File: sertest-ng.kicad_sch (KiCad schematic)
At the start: 52 parts, among them J101 SWD, J102 USB, SW101 Reset, U101 M24C64-RMN, U102 AMS1117-3.3, U103 STM32G431RBTx, U104 ATECC608B-MAVDA-S, U105 USBLC6-2SC6, Y101 8MHz, Y102 32k

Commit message: Swap USART1 RX/TX
Signed-off-by: Benedikt Spranger <b.spranger@linutronix.de>
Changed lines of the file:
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@@
 	)
 	(label "USART1_TX"
-		(at 226.06 134.62 180)
+		(at 226.06 132.08 180)
 		(effects
 			(font
@@
 	)
 	(label "USART1_RX"
-		(at 226.06 132.08 180)
-		(effects
-			(font
+		(at 226.06 134.62 180)
+		(effects
+			(font

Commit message: Fix USB signal swap
Signed-off-by: Benedikt Spranger <bene@eurovibes.org>
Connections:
- net USB_DM: now also U105.3 (I/O2); no longer U105.1 (I/O1)
- net USB_DP: now also U105.1 (I/O1); no longer U105.3 (I/O2)
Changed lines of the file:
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@@
 	)
 	(label "USB_DM"
-		(at 82.55 149.86 0)
+		(at 82.55 152.4 0)
 		(effects
 			(font
@@
 	)
 	(label "USB_DP"
-		(at 82.55 152.4 0)
+		(at 82.55 149.86 0)
 		(effects
 			(font

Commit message: Add USB termination resistors
Signed-off-by: Benedikt Spranger <b.spranger@linutronix.de>
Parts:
- added R108, R109: 33, Resistor_SMD:R_0402_1005Metric, symbol Device:R
- renumbered C107 to C101, C113 to C102, C114 to C103, C115 to C104, C106 to C105, C105 to C106, C108 to C107, C116 to C108, C101 to C110, C102 to C111, C110 to C112, C103 to C113, C111 to C114, C104 to C115, C112 to C116, D103 to D102, D104 to D103, D105 to D104, D106 to D105, D102 to D106, FB102 to FB101, FB101 to FB102, J102 to J101, J101 to J102, JP102 to JP101, JP101 to JP102, R111 to R102, R112 to R103, R105 to R104, R106 to R105, R104 to R106, R102 to R107, R107 to R110, R108 to R111, R109 to R112, R110 to R113, R103 to R114, U105 to U102, U102 to U105
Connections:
- net USB_DM: now also R109.1; no longer U102.3 (I/O2)
- net USB_DP: now also R108.2; no longer U102.1 (I/O1)
- new net: R108.1, U102.1 (I/O1)
- new net: R109.2, U102.3 (I/O2)

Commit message: Add BOOT0 support
Signed-off-by: Benedikt Spranger <b.spranger@linutronix.de>
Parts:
- added JP103: BOOT0, Jumper:SolderJumper-2_P1.3mm_Open_Pad1.0x1.5mm, symbol Jumper:Jumper_2_Open
- added R115: 10k, Resistor_SMD:R_0402_1005Metric, symbol Device:R
- R108, R109: Long Description (none) -> -55℃~+155℃ 33Ω 50V 62.5mW Thick Film Resistor ±1% ±100ppm/℃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; MF (none) -> UNI-ROYAL(Uniroyal Elec); MP (none) -> 0402WGF330JTCE; SupplLink (none) -> https://jlcpcb.com/partdetail/25848-0402WGF330JTCE/C25105; lcsc# (none) -> C25105
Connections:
- net +3V3: now also JP103.1 (A)
- net FDCAN1_RX: now also JP103.2 (B), R115.1
- net GND: now also R115.2

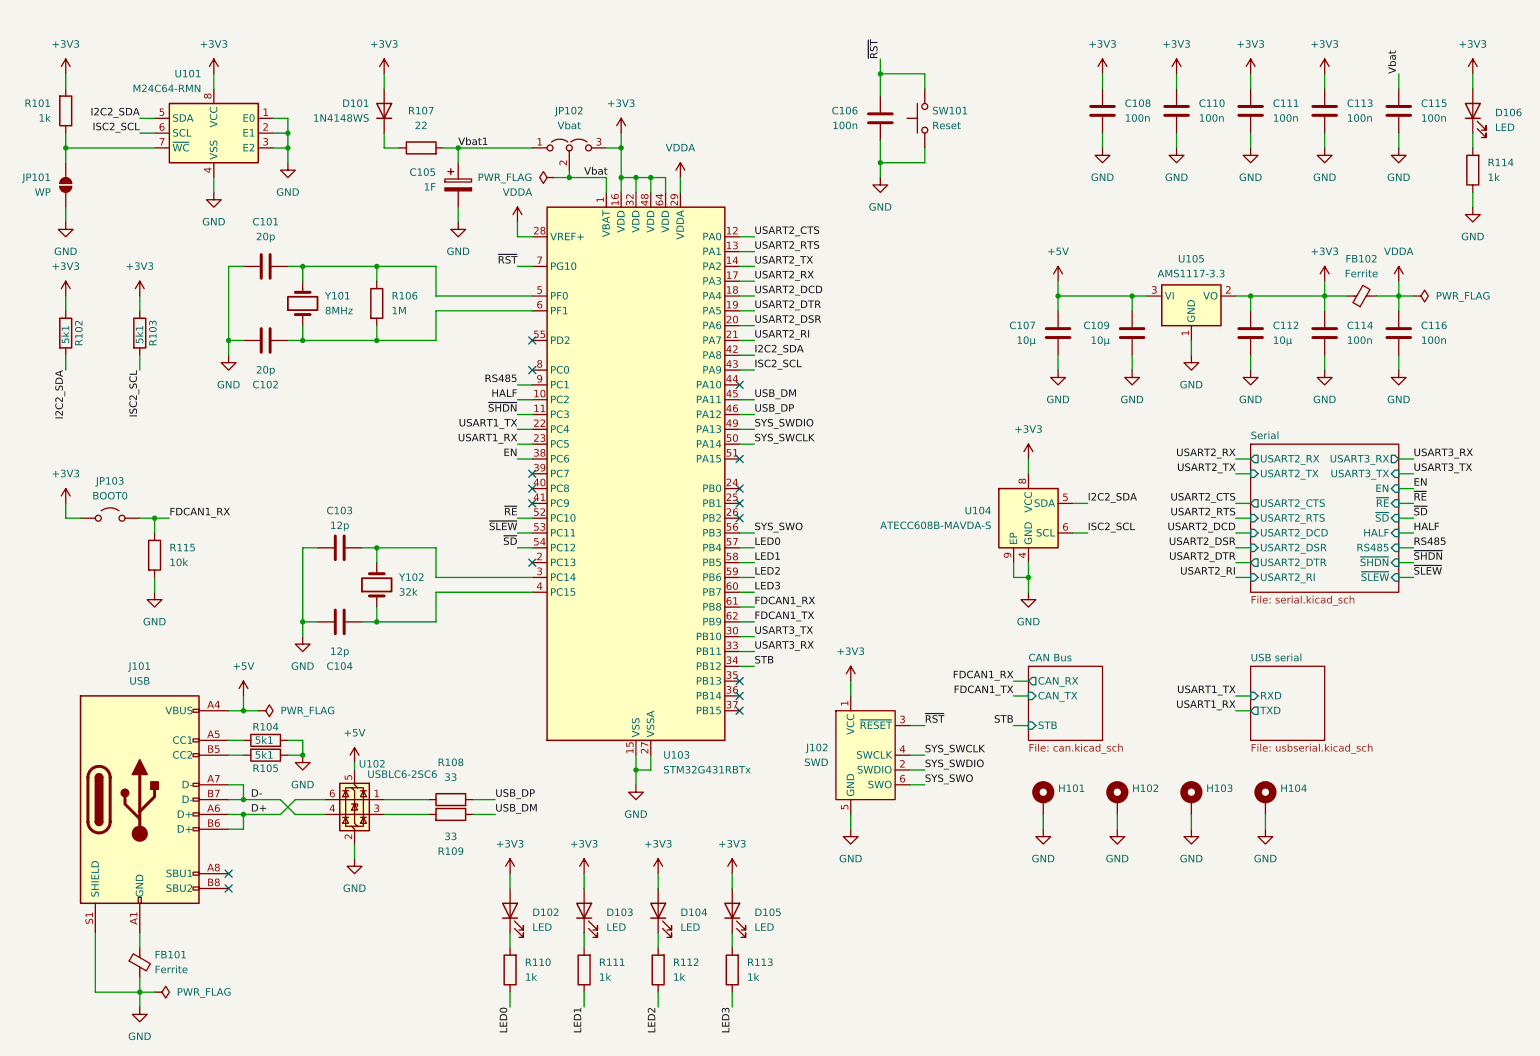
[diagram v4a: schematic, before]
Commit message: Add second EEPROM
Signed-off-by: Benedikt Spranger <b.spranger@linutronix.de>
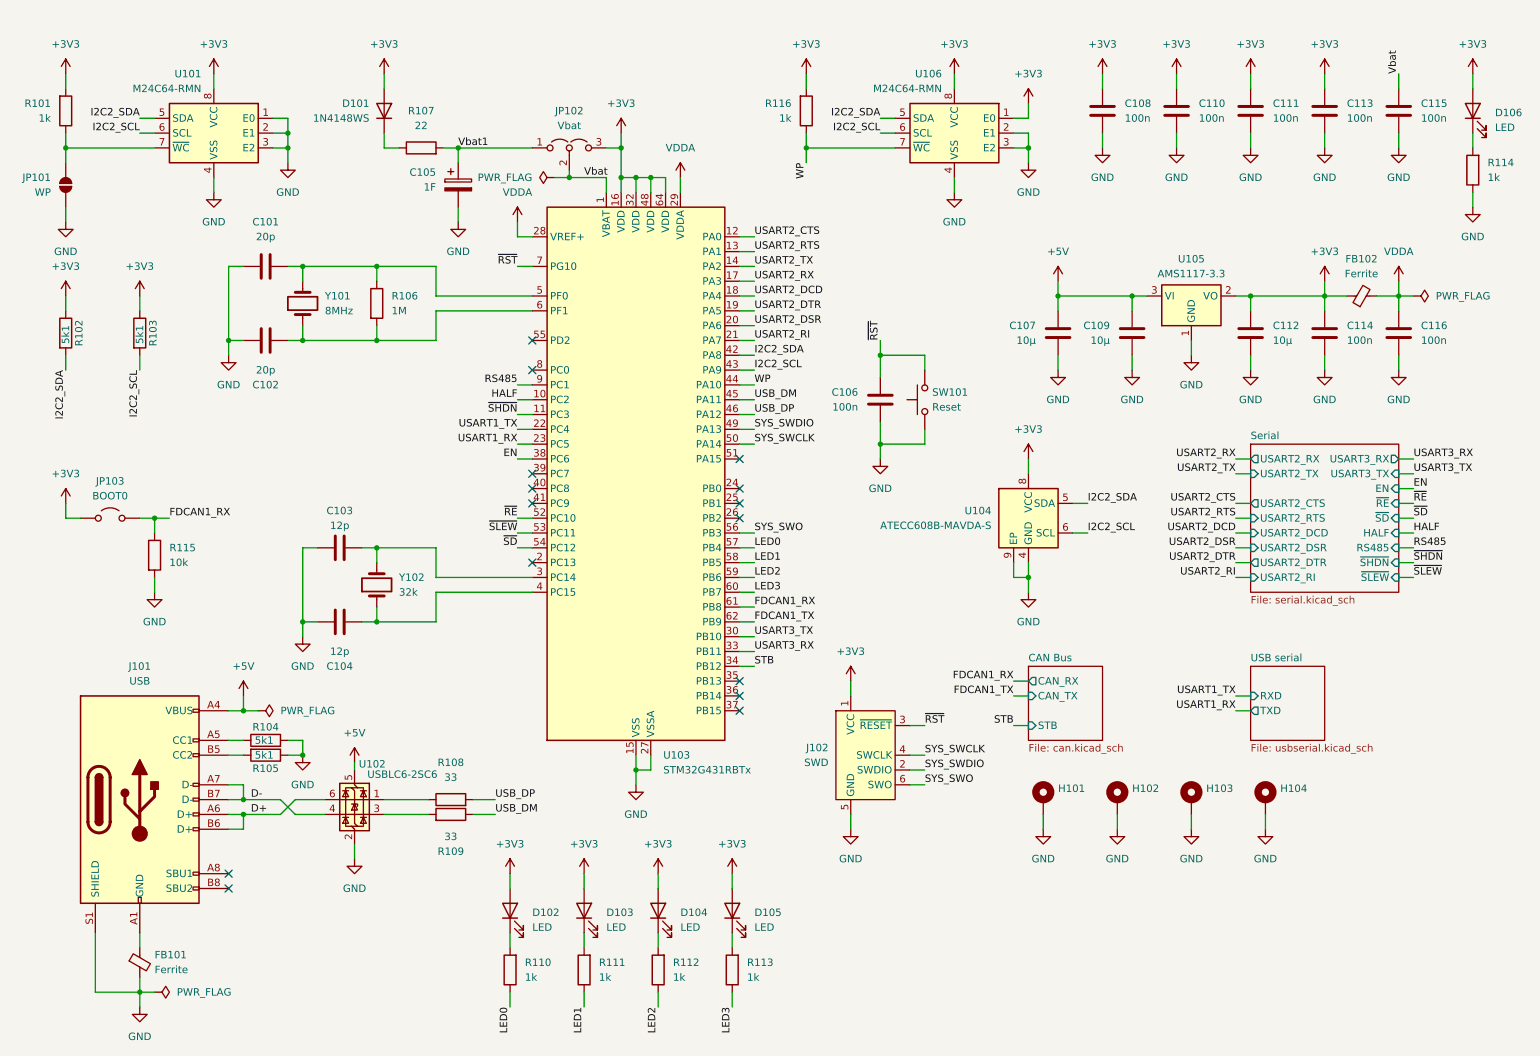
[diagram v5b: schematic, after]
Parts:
- added R116: 1k, Resistor_SMD:R_0402_1005Metric, symbol Device:R
- added U106: M24C64-RMN, Package_SO:SOIC-8_3.9x4.9mm_P1.27mm, symbol Memory_EEPROM:M24C02-RMN
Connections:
- net +3V3: now also R116.2, U106.1 (E0), U106.8 (VCC)
- net GND: now also U106.2 (E1), U106.3 (E2), U106.4 (VSS)
- net I2C2_SDA: now also U106.5 (SDA)
- net WP: now reaches U103.44 (PA10)
- net WP: now also R116.1, U106.7 (~{WC})
- net ISC2_SCL renamed I2C2_SCL
- net I2C2_SCL: now also U106.6 (SCL)
- no-connect marks 16 -> 15
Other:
- moved on the sheet: C106, SW101
